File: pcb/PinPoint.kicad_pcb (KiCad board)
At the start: 2 copper layers, 29.9 x 39.9 mm, 11 parts, among them SW1 SW_Push, U1 E73-2G4M08S-52833

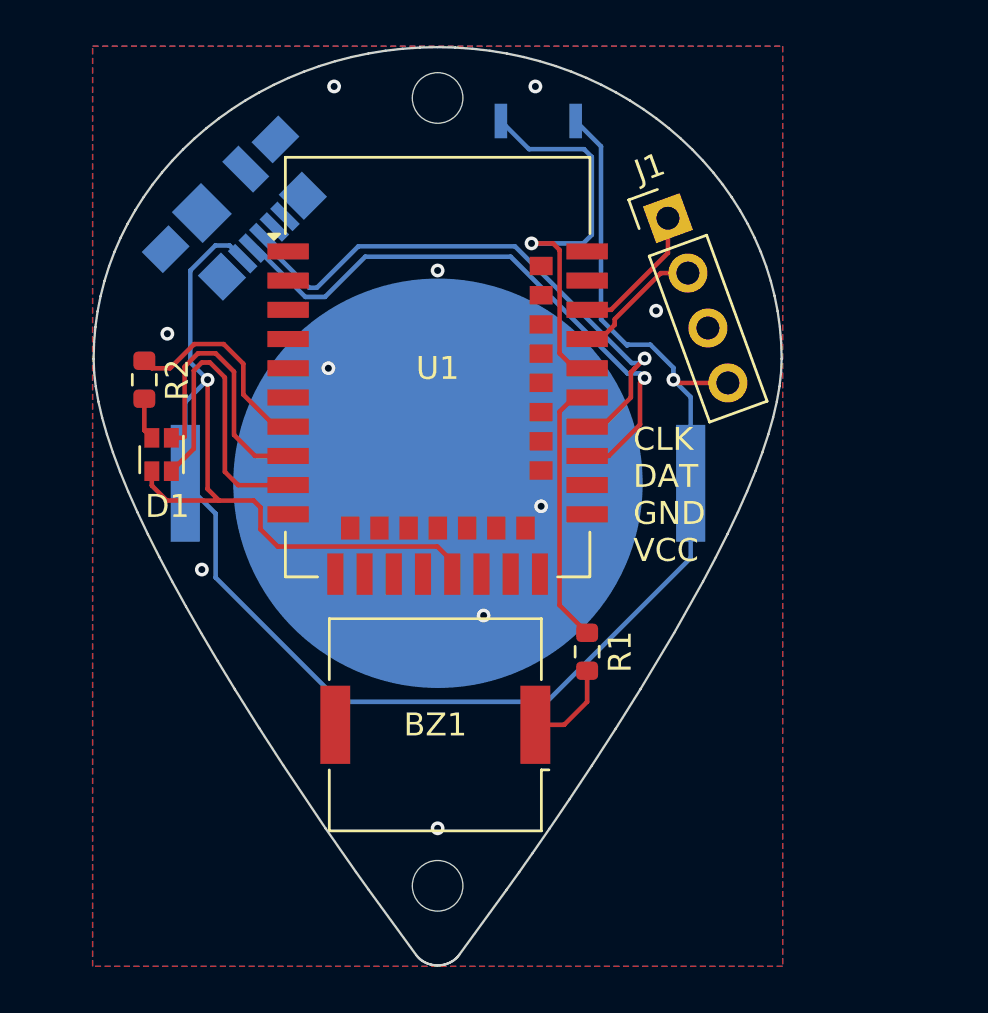
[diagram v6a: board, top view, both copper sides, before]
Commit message: Replace buzzer for active Add missing 3d models from lcsc
Signed-off-by: Devnol <pgkoutsoumanis@gmail.com>
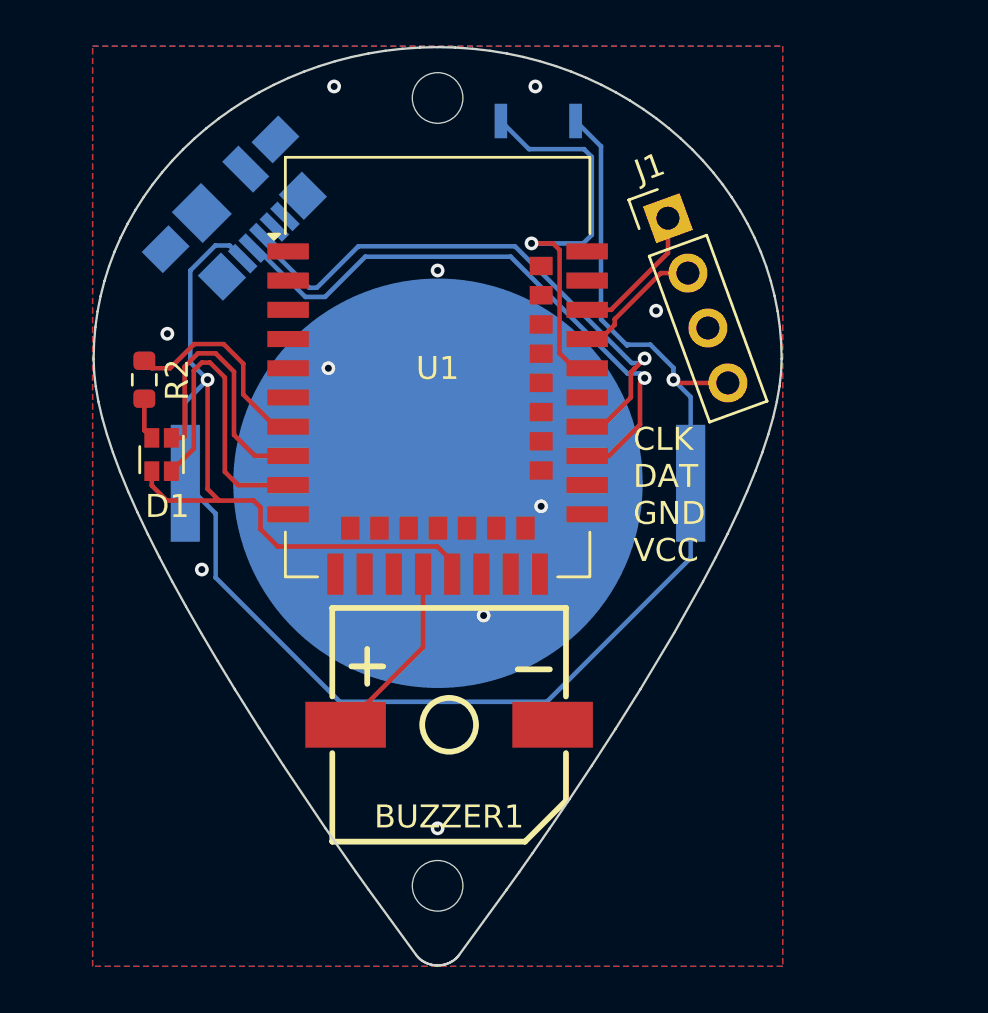
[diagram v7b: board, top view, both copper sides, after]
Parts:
- removed BZ1: Buzzer, Buzzer_Beeper:Buzzer_Murata_PKMCS0909E
- removed R1: 100Ω, Resistor_SMD:R_0603_1608Metric
- added BUZZER1: FST-9650B-3V, PinPoint_lib:BUZ-SMD_L9.6-W9.6-LS10.0-R, F.Cu at (107.2, 59.2)
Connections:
- U1 pad 17: unconnected-(U1-P1.09/TRACEDATA3-Pad17) -> Net-(BUZZER1-+)
- U1 pad 33: Net-(U1-P0.13) -> unconnected-(U1-P0.13-Pad33)
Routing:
- net Net-(U1-P0.13): track 11.6 -> 0.00 mm
- net Net-(BUZZER1-+): track 0.00 -> 7.94 mm
- net Net-(BZ1-+): track 4.01 -> 0.00 mm
